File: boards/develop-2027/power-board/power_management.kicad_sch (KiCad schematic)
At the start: 57 parts, among them Q1 PMOS, U3 LMR51430XDDCR, U4 LMR51430XDDCR, U5 SIC437AED-T1-GE3, U6 LM66100DCK, U7 INA4180A3IPWR, U8 LM66100DCK

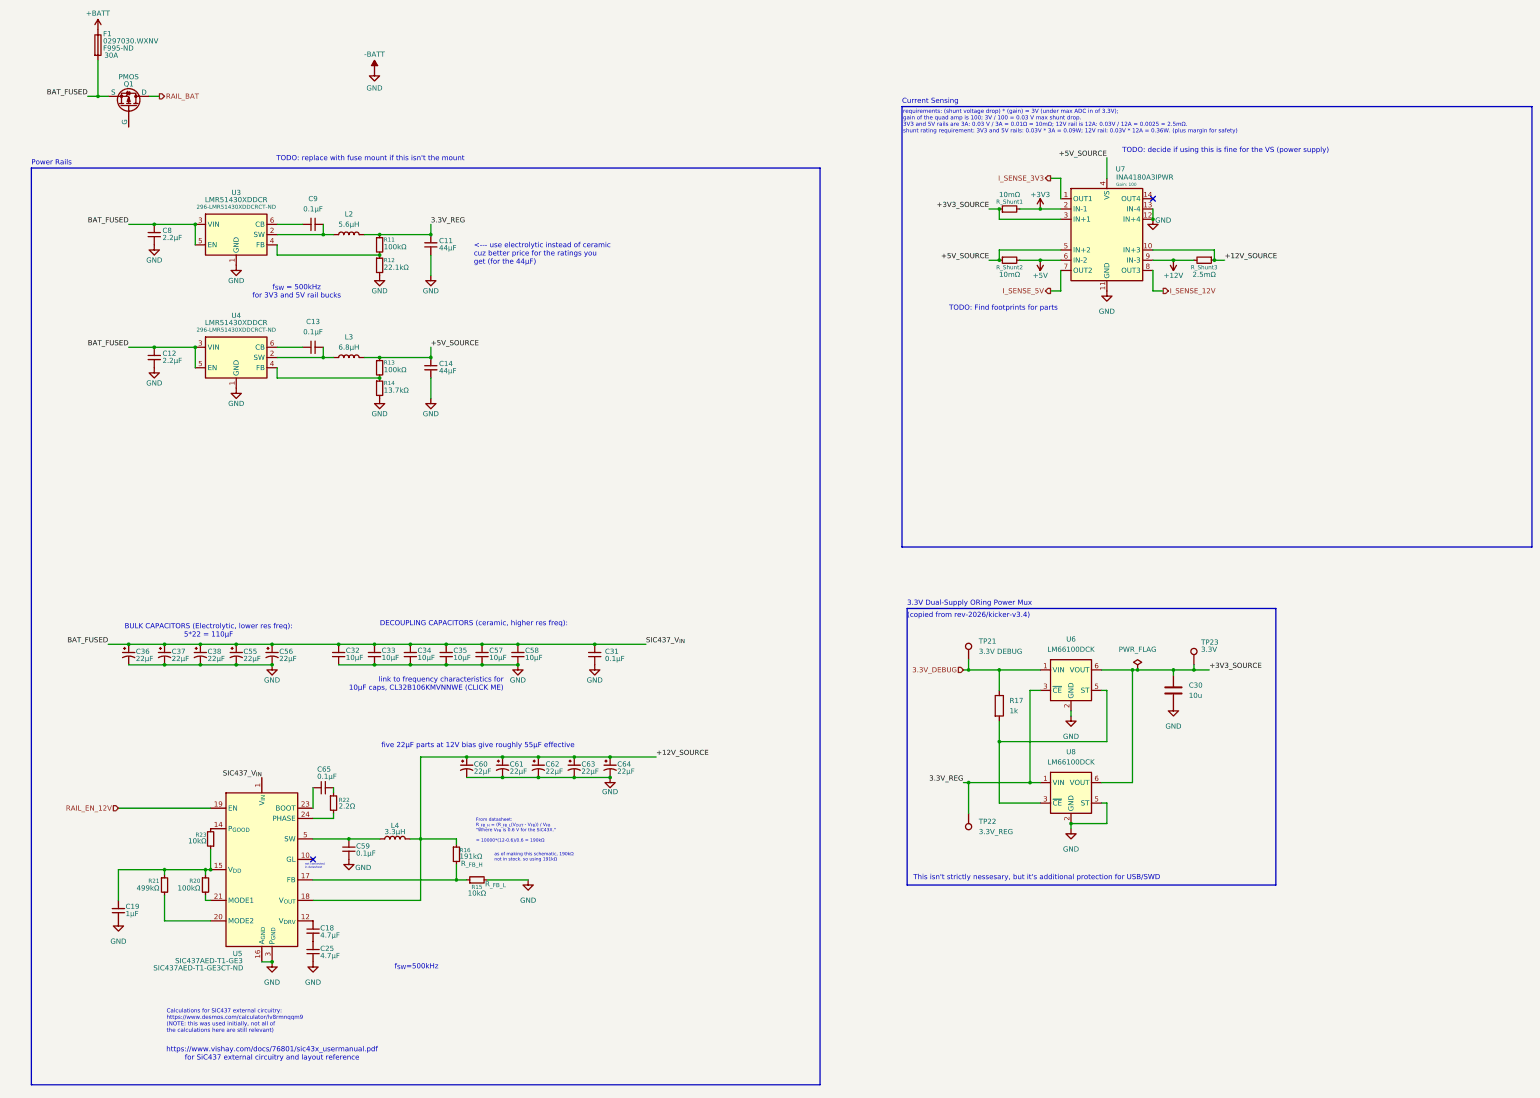
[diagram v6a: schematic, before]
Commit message: made high side power switch with pmos and nmos
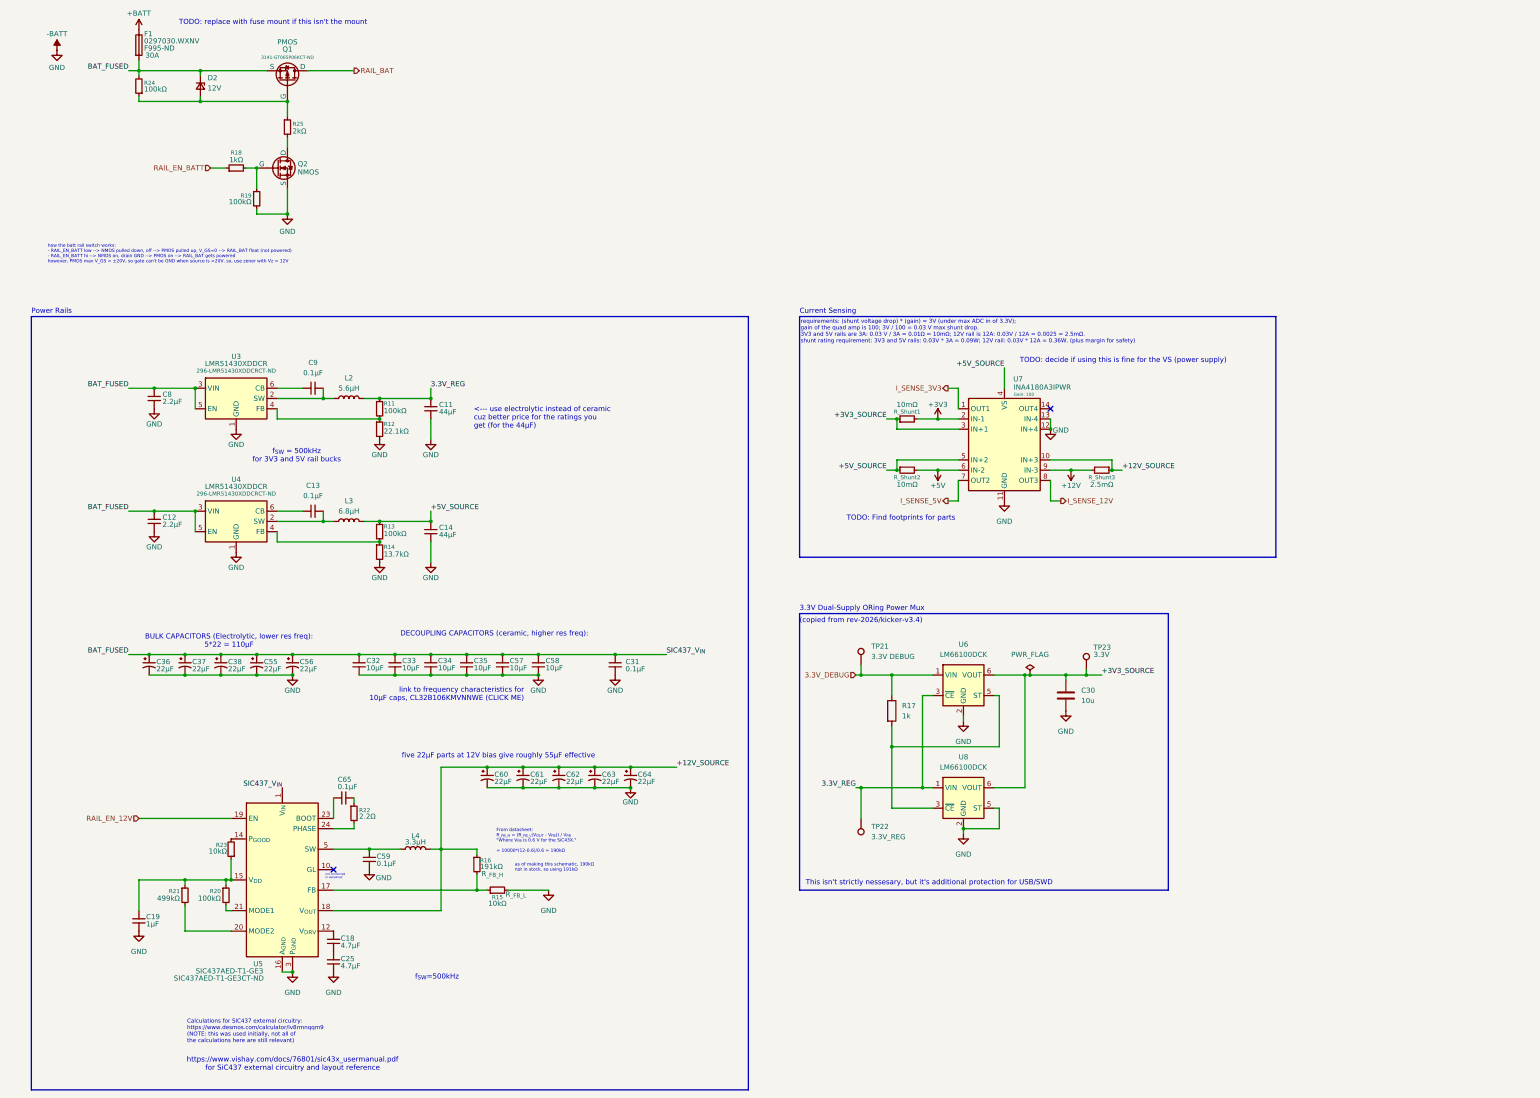
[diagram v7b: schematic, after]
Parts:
- added D2: 12V, symbol Device:D_Zener_Small
- added Q2: NMOS, Package_DFN_QFN:Nordic_AQFN-94-1EP_7x7mm_P0.4mm, symbol Simulation_SPICE:NMOS
- added R18: 1kΩ, Package_SO:TSSOP-20_4.4x6.5mm_P0.65mm, symbol Device:R_Small
- added R19, R24: 100kΩ, Package_SO:TSSOP-20_4.4x6.5mm_P0.65mm, symbol Device:R_Small
- added R25: 2kΩ, Package_SO:TSSOP-20_4.4x6.5mm_P0.65mm, symbol Device:R_Small
- C11, C14: DigiKey Part # (none) -> 399-A768EB476M1VLAE042CT-ND; DigikeyPart# 399-A768EB476M1VLAE042CT-ND -> (none); Part # (none) -> A768EB476M1VLAE042; Part# A768EB476M1VLAE042 -> (none)
- C12, C8: DigiKey Part # (none) -> 490-12332-1-ND; DigikeyPart# 490-12332-1-ND -> (none); Part # (none) -> GRT188R61H225KE13D; Part# GRT188R61H225KE13D -> (none)
- C13, C9: DigiKey Part # (none) -> 490-10700-1-ND; DigikeyPart# 490-10700-1-ND -> (none); Part # (none) -> GRM155R71H104KE14D; Part# GRM155R71H104KE14D -> (none)
- L2: DigiKey Part # (none) -> 4044-CSHB0540R-5R6MCT-ND; DigikeyPart# 4044-CSHB0540R-5R6MCT-ND -> (none); Part # (none) -> CSHB0540R-5R6M; Part# CSHB0540R-5R6M -> (none)
- L3: DigiKey Part # (none) -> 4044-CSBA1060-6R8MCT-ND; DigikeyPart# 4044-CSBA1060-6R8MCT-ND -> (none); Part # (none) -> CSBA1060-6R8M; Part# CSBA1060-6R8M -> (none)
- L4: DigiKey Part # (none) -> 4044-CSHB0540R-3R3MCT-ND; DigikeyPart# 4044-CSHB0540R-3R3MCT-ND -> (none); Part # (none) -> CSHB0540R-3R3M; Part# CSHB0540R-3R3M -> (none)
- Q1: DigiKey Part # (none) -> 3141-GT065P06KCT-ND; Part # (none) -> GT065P06K
- R11, R13: DigiKey Part # (none) -> 311-100KLRCT-ND; DigikeyPart# 311-100KLRCT-ND -> (none); Part # (none) -> RC0402FR-07100KL; Part# RC0402FR-07100KL -> (none)
- R12: DigiKey Part # (none) -> 311-22.1KHRCT-ND; DigikeyPart# 311-22.1KHRCT-ND -> (none); Part # (none) -> RC0603FR-0722K1L; Part# RC0603FR-0722K1L -> (none)
- R14: DigiKey Part # (none) -> 311-13.7KHRCT-ND; DigikeyPart# 311-13.7KHRCT-ND -> (none); Part # (none) -> RC0603FR-0713K7L; Part# RC0603FR-0713K7L -> (none)
- R_Shunt1, R_Shunt2: DigiKey Part # (none) -> P17098CT-ND; DigikeyPart# P17098CT-ND -> (none); Part # (none) -> ERJ-MS4HF10MU; Part# ERJ-MS4HF10MU -> (none)
- R_Shunt3: DigiKey Part # (none) -> 541-10116-1-ND; DigikeyPart# 541-10116-1-ND -> (none); Part # (none) -> WSL25122L500FEA; Part# WSL25122L500FEA -> (none)
- U6: footprint Package_TO_SOT_SMD:SOT-363_SC-70-6 -> Package_SO:DCK6_TEX-M; DigiKey Part # (none) -> 296-53541-1-ND; Digikey Part # LM66100DCK -> (none); Part # (none) -> LM66100DCKR
- U7: DigiKey Part # (none) -> 296-49096-1-ND; DigikeyPart# 296-49096-1-ND -> (none); Part # (none) -> INA4180A3IPWR; Part# INA4180A3IPWR -> (none)
- U8: footprint Package_TO_SOT_SMD:SOT-363_SC-70-6 -> Package_SO:DCK6_TEX-M; DigiKey Part # (none) -> 296-53541-1-ND; Part # (none) -> LM66100DCKR
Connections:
- net -BATT: now also Q2.3 (S), R19.2
- net BAT_FUSED: now also D2.1 (K), R24.2
- net at Q1.2 (G): now also D2.2 (A), R24.1, R25.1
- new net: Q2.2 (G), R18.2, R19.1
- new net: Q2.1 (D), R25.2
- new net RAIL_EN_BATT: R18.1
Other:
- note added: "how the batt rail switch works: - RAIL_EN_BATT low --> NMOS pulled down, off --> PMOS pulled up, V_GS=0 --> RAIL_BAT float (not powered) - RAIL_EN_BATT hi --> NMOS on, drain GND --> PMOS on --> RAIL_BAT gets powered however, PMOS max V_GS = ±20V, so gate can't be GND when source is >20V. so, use zener with Vz = 12V"
- moved on the sheet: C11, C12, C13, C14, C18, C19, C25, C30, C31, C32, C33, C34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

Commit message: all parts in (tentative)
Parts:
- C18, C25: DigiKey Part # 490-1864-1-ND -> 490-5915-1-ND; Part # GRM32ER71H475KA88L -> GRM155R60J475ME47D
- C19: DigiKey Part # 490-10017-1-ND -> 1276-1445-1-ND; Part # GRM155R61E105KA12D -> CL05A105KA5NQNC
- R17, R18: DigiKey Part # (none) -> 311-1.00KHRCT-ND; Part # (none) -> RC0603FR-071KL
- R19, R24: DigiKey Part # (none) -> 311-100KLRCT-ND; Part # (none) -> RC0402FR-07100KL
- R25: DigiKey Part # (none) -> 311-2.00KHRCT-ND; Part # (none) -> RC0603FR-072KL
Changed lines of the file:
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@@
 			)
 		)
-		(property "Part #" "GRM32ER71H475KA88L"
+		(property "Part #" "GRM155R60J475ME47D"
 			(at 90.17 245.11 0)
 			(hide yes)
@@
 			)
 		)
-		(property "DigiKey Part #" "490-1864-1-ND"
+		(property "DigiKey Part #" "490-5915-1-ND"
 			(at 90.17 245.11 0)
 			(hide yes)
@@
 			)
 		)
-		(property "Part #" "GRM32ER71H475KA88L"
+		(property "Part #" "GRM155R60J475ME47D"
 			(at 90.17 250.19 0)
 			(hide yes)
@@
 			)
 		)
-		(property "DigiKey Part #" "490-1864-1-ND"
+		(property "DigiKey Part #" "490-5915-1-ND"
 			(at 90.17 250.19 0)
 			(hide yes)
@@
 			)
 		)
-		(property "Datasheet" ""
+		(property "Datasheet" "https://yageogroup.com/content/datasheet/asset/file/PYU-RC_GROUP_51_ROHS_L"
 			(at 71.12 60.96 0)
 			(hide yes)
@@
 			)
 		)
+		(property "DigiKey Part #" "311-100KLRCT-ND"
+			(at 71.12 60.96 0)
+			(hide yes)
+			(show_name no)
+			(do_not_autoplace no)
+			(effects
+				(font
+					(size 1.27 1.27)
+				)
+			)
+		)
+		(property "Part #" "RC0402FR-07100KL"
+			(at 71.12 60.96 0)
+			(hide yes)
+			(show_name no)
+			(do_not_autoplace no)
+			(effects
+				(font
+					(size 1.27 1.27)
+				)
+			)
+		)
 		(pin "2"
 		)
@@
 			)
 		)
-		(property "Datasheet" ""
+		(property "Datasheet" "https://yageogroup.com/content/datasheet/asset/file/PYU-RC_GROUP_51_ROHS_L"
 			(at 78.74 43.18 0)
 			(hide yes)
@@
 			)
 		)
+		(property "DigiKey Part #" "311-2.00KHRCT-ND"
+			(at 78.74 43.18 0)
+			(hide yes)
+			(show_name no)
+			(do_not_autoplace no)
+			(effects
+				(font
+					(size 1.27 1.27)
+				)
+			)
+		)
+		(property "Part #" "RC0603FR-072KL"
+			(at 78.74 43.18 0)
+			(hide yes)
+			(show_name no)
+			(do_not_autoplace no)
+			(effects
+				(font
+					(size 1.27 1.27)
+				)
+			)
+		)
 		(pin "2"
 		)
@@
 			)
 		)
-		(property "Datasheet" ""
+		(property "Datasheet" "https://yageogroup.com/content/datasheet/asset/file/PYU-RC_GROUP_51_ROHS_L"
 			(at 228.6 187.96 0)
 			(hide yes)
@@
 			)
 		)
+		(property "DigiKey Part #" "311-1.00KHRCT-ND"
+			(at 228.6 187.96 0)
+			(hide yes)
+			(show_name no)
+			(do_not_autoplace no)
+			(effects
+				(font
+					(size 1.27 1.27)
+				)
+			)
+		)
+		(property "Part #" "RC0603FR-071KL"
+			(at 228.6 187.96 0)
+			(hide yes)
+			(show_name no)
+			(do_not_autoplace no)
+			(effects
+				(font
+					(size 1.27 1.27)
+				)
+			)
+		)
 		(pin "1"
 		)
@@
 			)
 		)
-		(property "Datasheet" ""
+		(property "Datasheet" "https://yageogroup.com/content/datasheet/asset/file/PYU-RC_GROUP_51_ROHS_L"
 			(at 66.04 53.34 0)
 			(hide yes)
@@
 			)
 		)
+		(property "DigiKey Part #" "311-1.00KHRCT-ND"
+			(at 66.04 53.34 90)
+			(hide yes)
+			(show_name no)
+			(do_not_autoplace no)
+			(effects
+				(font
+					(size 1.27 1.27)
+				)
+			)
+		)
+		(property "Part #" "RC0603FR-071KL"
+			(at 66.04 53.34 90)
+			(hide yes)
+			(show_name no)
+			(do_not_autoplace no)
+			(effects
+				(font
+					(size 1.27 1.27)
+				)
+			)
+		)
 		(pin "2"
 		)
@@
 			)
 		)
-		(property "Datasheet" ""
+		(property "Datasheet" "https://yageogroup.com/content/datasheet/asset/file/PYU-RC_GROUP_51_ROHS_L"
 			(at 41.91 33.02 0)
 			(hide yes)
@@
 			)
 		)
+		(property "DigiKey Part #" "311-100KLRCT-ND"
+			(at 41.91 33.02 0)
+			(hide yes)
+			(show_name no)
+			(do_not_autoplace no)
+			(effects
+				(font
+					(size 1.27 1.27)
+				)
+			)
+		)
+		(property "Part #" "RC0402FR-07100KL"
+			(at 41.91 33.02 0)
+			(hide yes)
+			(show_name no)
+			(do_not_autoplace no)
+			(effects
+				(font
+					(size 1.27 1.27)
+				)
+			)
+		)
 		(pin "2"
 		)
@@
 			)
 		)
-		(property "Datasheet" ""
+		(property "Datasheet" "https://mm.digikey.com/Volume0/opasdata/d220001/medias/docus/41/CL05A105KA5NQNC.pdf"
 			(at 41.91 240.03 0)
 			(hide yes)
@@
 			)
 		)
-		(property "Part #" "GRM155R61E105KA12D"
+		(property "Part #" "CL05A105KA5NQNC"
 			(at 41.91 240.03 0)
 			(hide yes)
@@
 			)
 		)
-		(property "DigiKey Part #" "490-10017-1-ND"
+		(property "DigiKey Part #" "1276-1445-1-ND"
 			(at 41.91 240.03 0)
 			(hide yes)
